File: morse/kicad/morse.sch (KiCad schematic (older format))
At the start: 3 parts

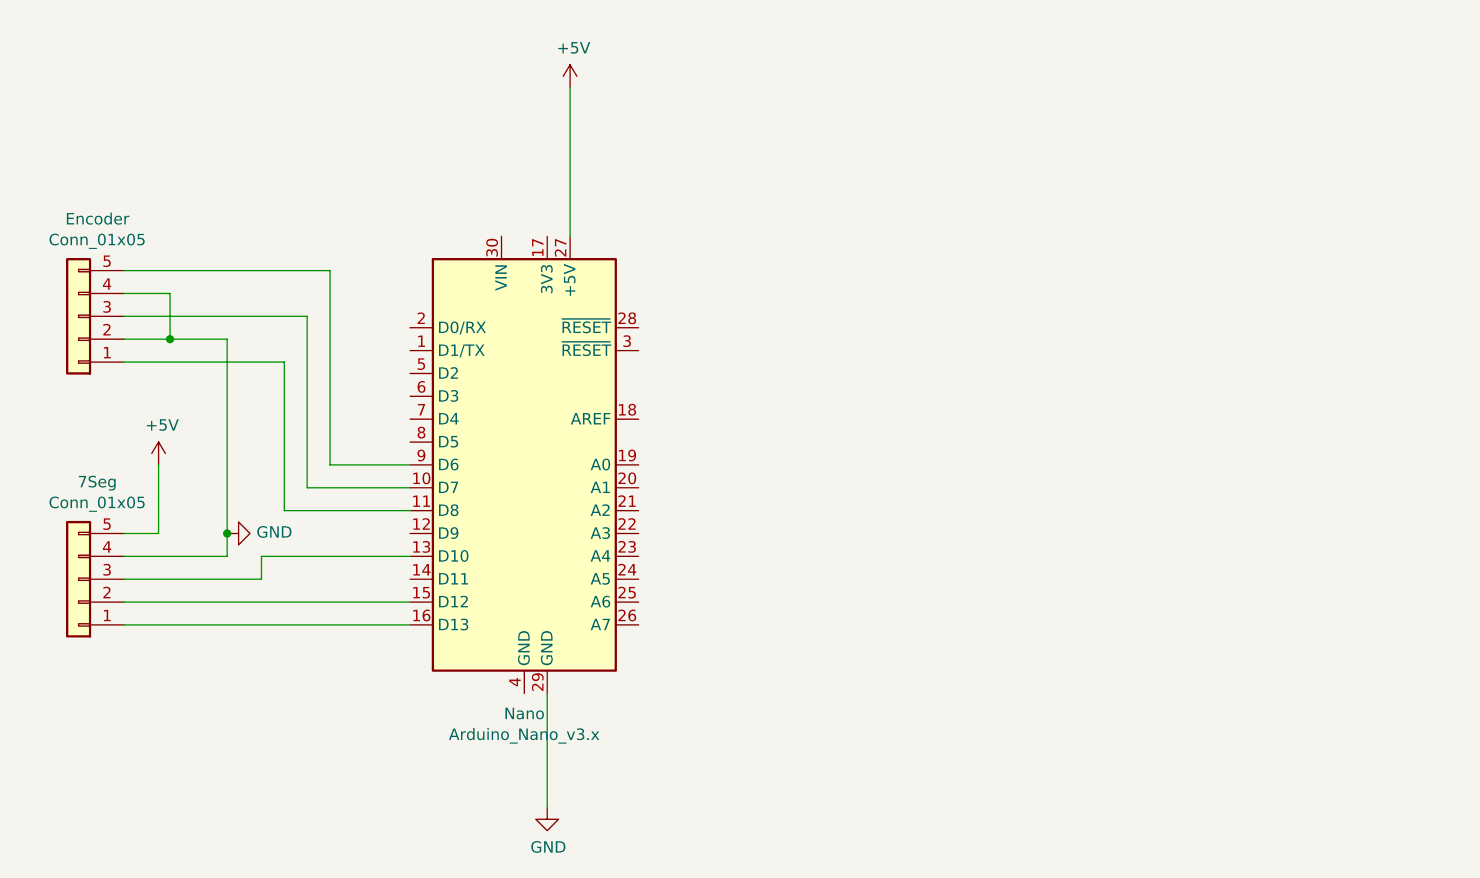
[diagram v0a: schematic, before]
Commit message: updating maze symlinks and added rotary encoder to kicad
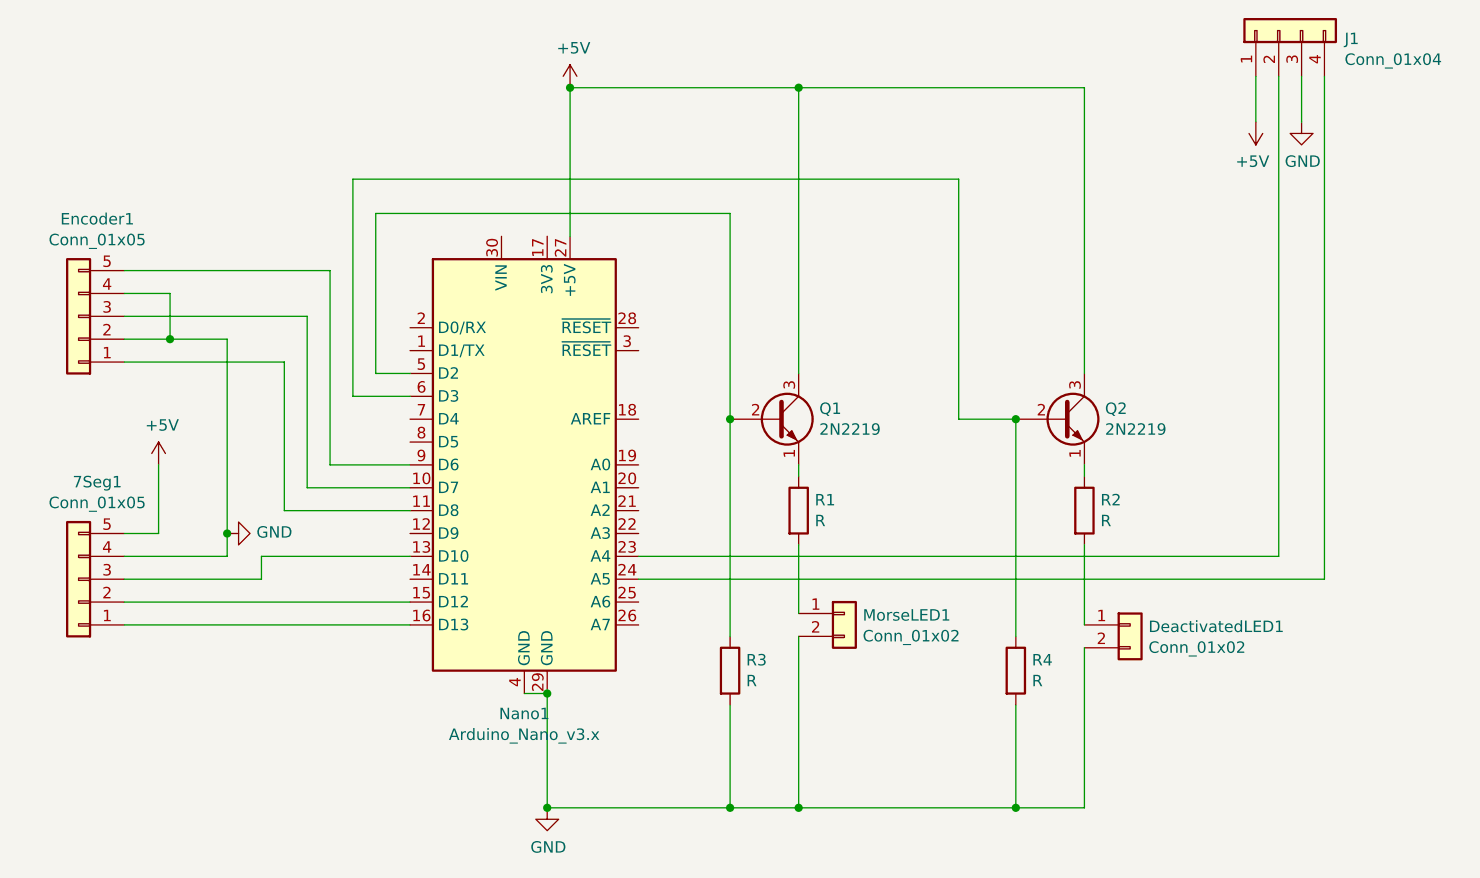
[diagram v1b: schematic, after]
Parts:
- added DeactivatedLED1, MorseLED1: Conn_01x02, Connector_PinHeader_2.54mm:PinHeader_1x02_P2.54mm_Vertical, symbol Connector_Generic:Conn_01x02
- added J1: Conn_01x04, Connector_PinHeader_2.54mm:PinHeader_1x04_P2.54mm_Vertical, symbol Connector_Generic:Conn_01x04
- added Q1, Q2: 2N2219, Package_TO_SOT_THT:TO-39-3, symbol Transistor_BJT:2N2219
- added R1, R2, R3, R4: R, Resistor_THT:R_Axial_DIN0309_L9.0mm_D3.2mm_P12.70mm_Horizontal, symbol Device:R
- 7Seg1: renamed from 7Seg; footprint (none) -> Connector_PinHeader_2.54mm:PinHeader_1x05_P2.54mm_Vertical
- Encoder1: renamed from Encoder; footprint (none) -> Connector_PinHeader_2.54mm:PinHeader_1x05_P2.54mm_Vertical
- renumbered Nano to Nano1
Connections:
- net +5V: now also J1.1 (Pin_1), Q1.3 (C), Q2.3 (C)
- net GND: now also Nano1.4 (GND), DeactivatedLED1.2 (Pin_2), J1.3 (Pin_3), MorseLED1.2 (Pin_2), R3.2, R4.2
- net at Nano1.23 (A4): now also J1.2 (Pin_2)
- net at Nano1.24 (A5): now also J1.4 (Pin_4)
- net at Nano1.5 (D2): now also Q1.2 (B), R3.1
- net at Nano1.6 (D3): now also Q2.2 (B), R4.1
- new net: Q1.1 (E), R1.1
- new net: MorseLED1.1 (Pin_1), R1.2
- new net: DeactivatedLED1.1 (Pin_1), R2.2
- new net: Q2.1 (E), R2.1
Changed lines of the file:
@@
 $EndDescr
 $Comp
-L power:+5V #PWR?
+L power:+5V #PWR0101
 U 1 1 6103FD1C
 P 5300 1600
-F 0 "#PWR?" H 5300 1450 50  0001 C CNN
+F 0 "#PWR0101" H 5300 1450 50  0001 C CNN
 F 1 "+5V" H 5315 1773 50  0000 C CNN
 F 2 "" H 5300 1600 50  0001 C CNN
@@
 	5300 1600 5300 2250
 $Comp
-L power:GND #PWR?
+L power:GND #PWR0102
 U 1 1 61041E97
 P 5200 4750
-F 0 "#PWR?" H 5200 4500 50  0001 C CNN
+F 0 "#PWR0102" H 5200 4500 50  0001 C CNN
 F 1 "GND" H 5205 4577 50  0000 C CNN
 F 2 "" H 5200 4750 50  0001 C CNN
@@
 	5200 4250 5200 4750
 $Comp
-L Connector_Generic:Conn_01x05 7Seg
+L Connector_Generic:Conn_01x05 7Seg1
 U 1 1 61042CBA
 P 3150 3750
-F 0 "7Seg" H 3068 3325 50  0000 C CNN
+F 0 "7Seg1" H 3068 3325 50  0000 C CNN
 F 1 "Conn_01x05" H 3068 3416 50  0000 C CNN
-F 2 "" H 3150 3750 50  0001 C CNN
+F 2 "Connector_PinHeader_2.54mm:PinHeader_1x05_P2.54mm_Vertical" H 3150 3750 50  0001 C CNN
 F 3 "~" H 3150 3750 50  0001 C CNN
 	1    3150 3750
@@
 	3950 3750 3350 3750
 $Comp
-L power:+5V #PWR?
+L power:+5V #PWR0103
 U 1 1 61044D5A
 P 3500 3250
-F 0 "#PWR?" H 3500 3100 50  0001 C CNN
+F 0 "#PWR0103" H 3500 3100 50  0001 C CNN
 F 1 "+5V" H 3515 3423 50  0000 C CNN
 F 2 "" H 3500 3250 50  0001 C CNN
@@
 	3500 3550 3500 3250
 $Comp
-L Connector_Generic:Conn_01x05 Encoder
+L Connector_Generic:Conn_01x05 Encoder1
 U 1 1 61045C91
 P 3150 2600
-F 0 "Encoder" H 3068 2175 50  0000 C CNN
+F 0 "Encoder1" H 3068 2175 50  0000 C CNN
 F 1 "Conn_01x05" H 3068 2266 50  0000 C CNN
-F 2 "" H 3150 2600 50  0001 C CNN
+F 2 "Connector_PinHeader_2.54mm:PinHeader_1x05_P2.54mm_Vertical" H 3150 2600 50  0001 C CNN
 F 3 "~" H 3150 2600 50  0001 C CNN
 	1    3150 2600
@@
 	4050 3450 4600 3450
 $Comp
-L power:GND #PWR?
+L power:GND #PWR0104
 U 1 1 61045251
 P 3800 3550
-F 0 "#PWR?" H 3800 3300 50  0001 C CNN
+F 0 "#PWR0104" H 3800 3300 50  0001 C CNN
 F 1 "GND" V 3805 3422 50  0000 R CNN
 F 2 "" H 3800 3550 50  0001 C CNN
@@
 $EndComp
 $Comp
-L MCU_Module:Arduino_Nano_v3.x Nano
+L MCU_Module:Arduino_Nano_v3.x Nano1
 U 1 1 6103F115
 P 5100 3250
-F 0 "Nano" H 5100 2161 50  0000 C CNN
+F 0 "Nano1" H 5100 2161 50  0000 C CNN
 F 1 "Arduino_Nano_v3.x" H 5100 2070 50  0000 C CNN
 F 2 "Module:Arduino_Nano" H 5100 3250 50  0001 C CIN
@@
 	1    0    0    -1
 $EndComp
+$Comp
+L Transistor_BJT:2N2219 Q1
+U 1 1 6104D7BF
+P 6200 3050
+F 0 "Q1" H 6390 3096 50  0000 L CNN
+F 1 "2N2219" H 6390 3005 50  0000 L CNN
+F 2 "Package_TO_SOT_THT:TO-39-3" H 6400 2975 50  0001 L CIN
+F 3 "http://www.onsemi.com/pub_link/Collateral/2N2219-D.PDF" H 6200 3050 50  0001 L CNN
+	1    6200 3050
+	1    0    0    -1
+$EndComp
+Wire Wire Line
+	4600 2850 4450 2850
+Wire Wire Line
+	4450 2850 4450 2150
+Wire Wire Line
+	4450 2150 6000 2150
+Wire Wire Line
+	6000 2150 6000 3050
+Wire Wire Line
+	6300 2850 6300 1600
+Wire Wire Line
+	6300 1600 5300 1600
+Connection ~ 5300 1600
+$Comp
+L Connector_Generic:Conn_01x02 MorseLED1
+U 1 1 610551C1
+P 6500 3900
+F 0 "MorseLED1" H 6580 3892 50  0000 L CNN
+F 1 "Conn_01x02" H 6580 3801 50  0000 L CNN
+F 2 "Connector_PinHeader_2.54mm:PinHeader_1x02_P2.54mm_Vertical" H 6500 3900 50  0001 C CNN
+F 3 "~" H 6500 3900 50  0001 C CNN
+	1    6500 3900
+	1    0    0    -1
+$EndComp
+$Comp
+L Connector_Generic:Conn_01x02 DeactivatedLED1
+U 1 1 6105576B
+P 7750 3950
+F 0 "DeactivatedLED1" H 7830 3942 50  0000 L CNN
+F 1 "Conn_01x02" H 7830 3851 50  0000 L CNN
+F 2 "Connector_PinHeader_2.54mm:PinHeader_1x02_P2.54mm_Vertical" H 7750 3950 50  0001 C CNN
+F 3 "~" H 7750 3950 50  0001 C CNN
+	1    7750 3950
+	1    0    0    -1
+$EndComp
+Wire Wire Line
+	6300 4000 6300 4750
+Wire Wire Line
+	6300 4750 6000 4750
+Connection ~ 5200 4750
+Wire Wire Line
+	7550 4050 7550 4750
+Wire Wire Line
+	7550 4750 7250 4750
+Connection ~ 6300 4750
+Wire Wire Line
+	7550 1600 6300 1600
+Connection ~ 6300 1600
+Wire Wire Line
+	7000 3050 7000 2000
+Wire Wire Line
+	7000 2000 4350 2000
+Wire Wire Line
+	4350 2000 4350 2950
+Wire Wire Line
+	4350 2950 4600 2950
+$Comp
+L Connector_Generic:Conn_01x04 J1
+U 1 1 6105BDAA
+P 8400 1350
+F 0 "J1" V 8364 1062 50  0000 R CNN
+F 1 "Conn_01x04" V 8273 1062 50  0000 R CNN
+F 2 "Connector_PinHeader_2.54mm:PinHeader_1x04_P2.54mm_Vertical" H 8400 1350 50  0001 C CNN
+F 3 "~" H 8400 1350 50  0001 C CNN
+	1    8400 1350
+	0    -1   -1   0
+$EndComp
+$Comp
+L power:GND #PWR0105
+U 1 1 6105C619
+P 8500 1750
+F 0 "#PWR0105" H 8500 1500 50  0001 C CNN
+F 1 "GND" H 8505 1577 50  0000 C CNN
+F 2 "" H 8500 1750 50  0001 C CNN
+F 3 "" H 8500 1750 50  0001 C CNN
+	1    8500 1750
+	1    0    0    -1
+$EndComp
+$Comp
+L power:+5V #PWR0106
+U 1 1 6105CC5E
+P 8300 1750
+F 0 "#PWR0106" H 8300 1600 50  0001 C CNN
+F 1 "+5V" H 8315 1923 50  0000 C CNN
+F 2 "" H 8300 1750 50  0001 C CNN
+F 3 "" H 8300 1750 50  0001 C CNN
+	1    8300 1750
+	-1   0    0    1
+$EndComp
+Wire Wire Line
+	8300 1550 8300 1750
+Wire Wire Line
+	8500 1550 8500 1750
+Wire Wire Line
+	8400 1550 8400 3650
+Wire Wire Line
+	8400 3650 5600 3650
+Wire Wire Line
+	7550 2850 7550 1600
+Wire Wire Line
+	7250 3050 7000 3050
+$Comp
+L Transistor_BJT:2N2219 Q2
+U 1 1 6105728C
+P 7450 3050
+F 0 "Q2" H 7640 3096 50  0000 L CNN
+F 1 "2N2219" H 7640 3005 50  0000 L CNN
+F 2 "Package_TO_SOT_THT:TO-39-3" H 7650 2975 50  0001 L CIN
+F 3 "http://www.onsemi.com/pub_link/Collateral/2N2219-D.PDF" H 7450 3050 50  0001 L CNN
+	1    7450 3050
+	1    0    0    -1
+$EndComp
+Wire Wire Line
+	7550 3600 7550 3950
+Wire Wire Line
+	7550 3250 7550 3300
+$Comp
+L Device:R R2
+U 1 1 61056D92
+P 7550 3450
+F 0 "R2" H 7620 3496 50  0000 L CNN
+F 1 "R" H 7620 3405 50  0000 L CNN
+F 2 "Resistor_THT:R_Axial_DIN0309_L9.0mm_D3.2mm_P12.70mm_Horizontal" V 7480 3450 50  0001 C CNN
+F 3 "~" H 7550 3450 50  0001 C CNN
+	1    7550 3450
+	1    0    0    -1
+$EndComp
+Wire Wire Line
+	8600 1550 8600 3750
+Wire Wire Line
+	8600 3750 5600 3750
+$Comp
+L Device:R R1
+U 1 1 6104E96F
+P 6300 3450
+F 0 "R1" H 6370 3496 50  0000 L CNN
+F 1 "R" H 6370 3405 50  0000 L CNN
+F 2 "Resistor_THT:R_Axial_DIN0309_L9.0mm_D3.2mm_P12.70mm_Horizontal" V 6230 3450 50  0001 C CNN
+F 3 "~" H 6300 3450 50  0001 C CNN
+	1    6300 3450
+	1    0    0    -1
+$EndComp
+Wire Wire Line
+	6300 3250 6300 3300
+Wire Wire Line
+	6300 3600 6300 3900
+Wire Wire Line
+	5100 4250 5200 4250
+Connection ~ 5200 4250
+$Comp
+L Device:R R3
+U 1 1 6108410E
+P 6000 4150
+F 0 "R3" H 6070 4196 50  0000 L CNN
+F 1 "R" H 6070 4105 50  0000 L CNN
+F 2 "Resistor_THT:R_Axial_DIN0309_L9.0mm_D3.2mm_P12.70mm_Horizontal" V 5930 4150 50  0001 C CNN
+F 3 "~" H 6000 4150 50  0001 C CNN
+	1    6000 4150
+	1    0    0    -1
+$EndComp
+$Comp
+L Device:R R4
+U 1 1 61084C3D
+P 7250 4150
+F 0 "R4" H 7320 4196 50  0000 L CNN
+F 1 "R" H 7320 4105 50  0000 L CNN
+F 2 "Resistor_THT:R_Axial_DIN0309_L9.0mm_D3.2mm_P12.70mm_Horizontal" V 7180 4150 50  0001 C CNN
+F 3 "~" H 7250 4150 50  0001 C CNN
+	1    7250 4150
+	1    0    0    -1
+$EndComp
+Wire Wire Line
+	6000 3050 6000 4000
+Connection ~ 6000 3050
+Wire Wire Line
+	7250 4000 7250 3050
+Connection ~ 7250 3050
+Wire Wire Line
+	7250 4300 7250 4750
+Connection ~ 7250 4750
+Wire Wire Line
+	7250 4750 6300 4750
+Wire Wire Line
+	6000 4300 6000 4750
+Connection ~ 6000 4750
+Wire Wire Line
+	6000 4750 5200 4750
 $EndSCHEMATC

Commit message: updating morse pcb layout
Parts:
- removed DeactivatedLED1, MorseLED1: Conn_01x02, Connector_PinHeader_2.54mm:PinHeader_1x02_P2.54mm_Vertical, symbol Connector_Generic:Conn_01x02
- removed Encoder1: Conn_01x05, Connector_PinHeader_2.54mm:PinHeader_1x05_P2.54mm_Vertical, symbol Connector_Generic:Conn_01x05
- added Disarmed1: LED, LED_THT:LED_D5.0mm, symbol Device:LED
- added Encoder1: Rotary_Encoder_Switch, Rotary_Encoder:RotaryEncoder_Alps_EC11E-Switch_Vertical_H20mm_CircularMountingHoles, symbol Device:Rotary_Encoder_Switch
- added Morse1: LED, LED_THT:LED_D10.0mm, symbol Device:LED
- renumbered J1 to Master1
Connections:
- net GND: now also Disarmed1.1 (K), Encoder1.C, Encoder1.S2, Morse1.1 (K)
- net at Nano1.10 (D7): now also Encoder1.B
- net at Nano1.11 (D8): now also Encoder1.A
- net at Nano1.23 (A4): now also Master1.4 (Pin_4); no longer Master1.2 (Pin_2)
- net at Nano1.24 (A5): now also Master1.2 (Pin_2); no longer Master1.4 (Pin_4)
- net at Nano1.9 (D6): now also Encoder1.S1
- net at R1.2: now also Morse1.2 (A)
- net at R2.2: now also Disarmed1.2 (A)
